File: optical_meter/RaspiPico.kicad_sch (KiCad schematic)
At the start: 7 parts, among them J4 Conn_02x03, U4 Pico

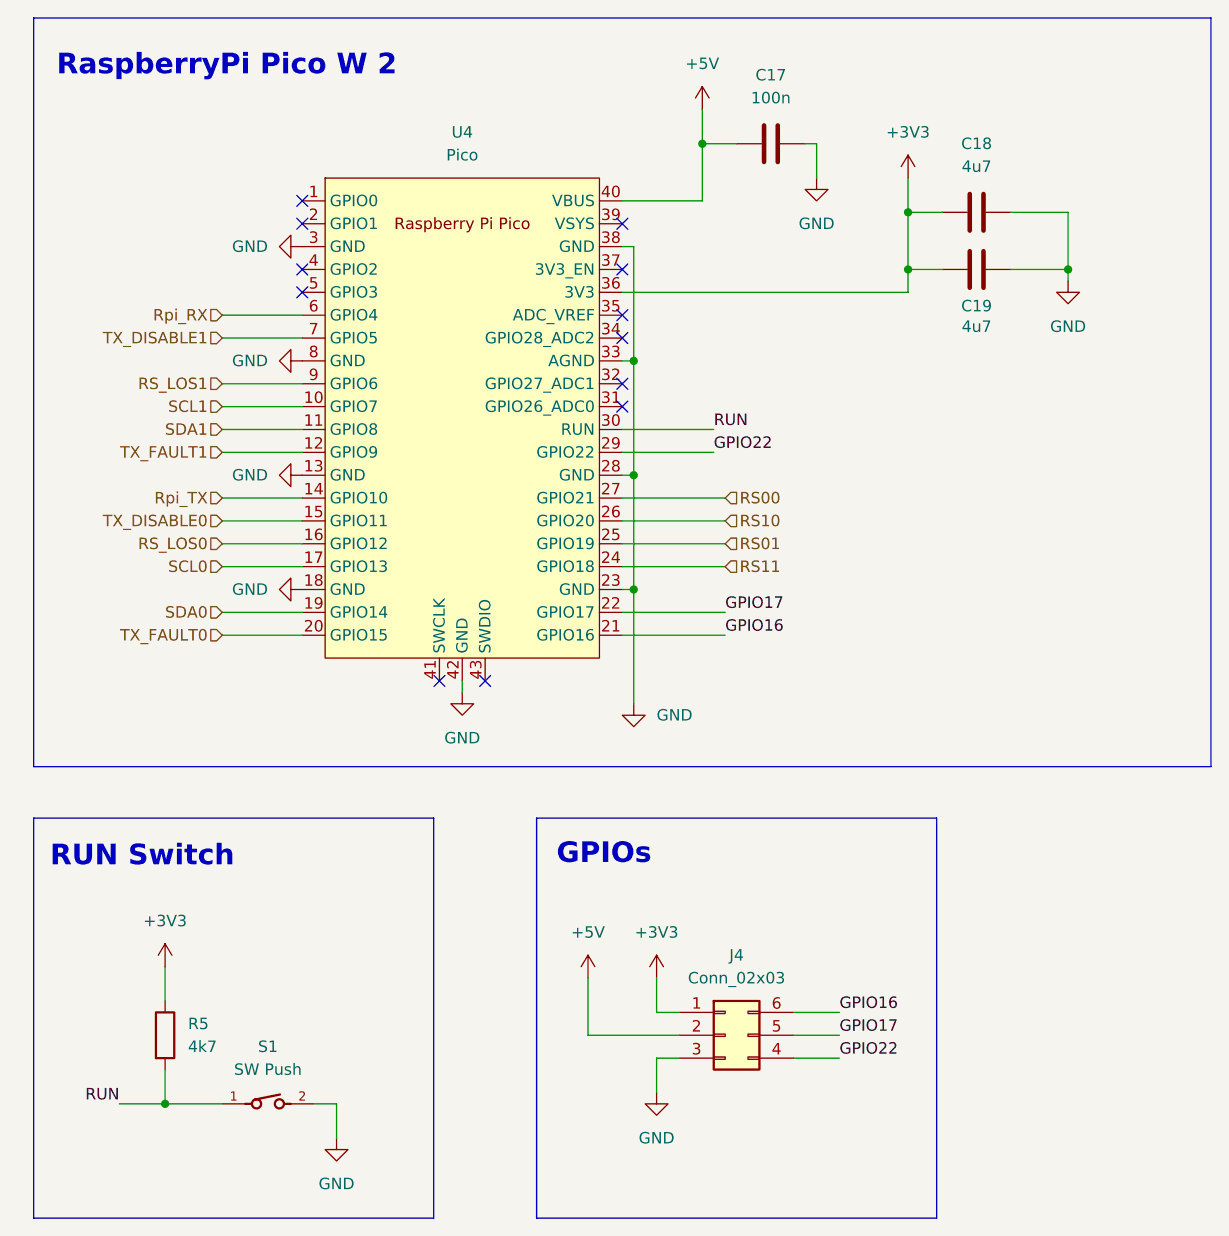
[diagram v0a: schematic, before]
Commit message: Cosmetic changes to schematic sheet
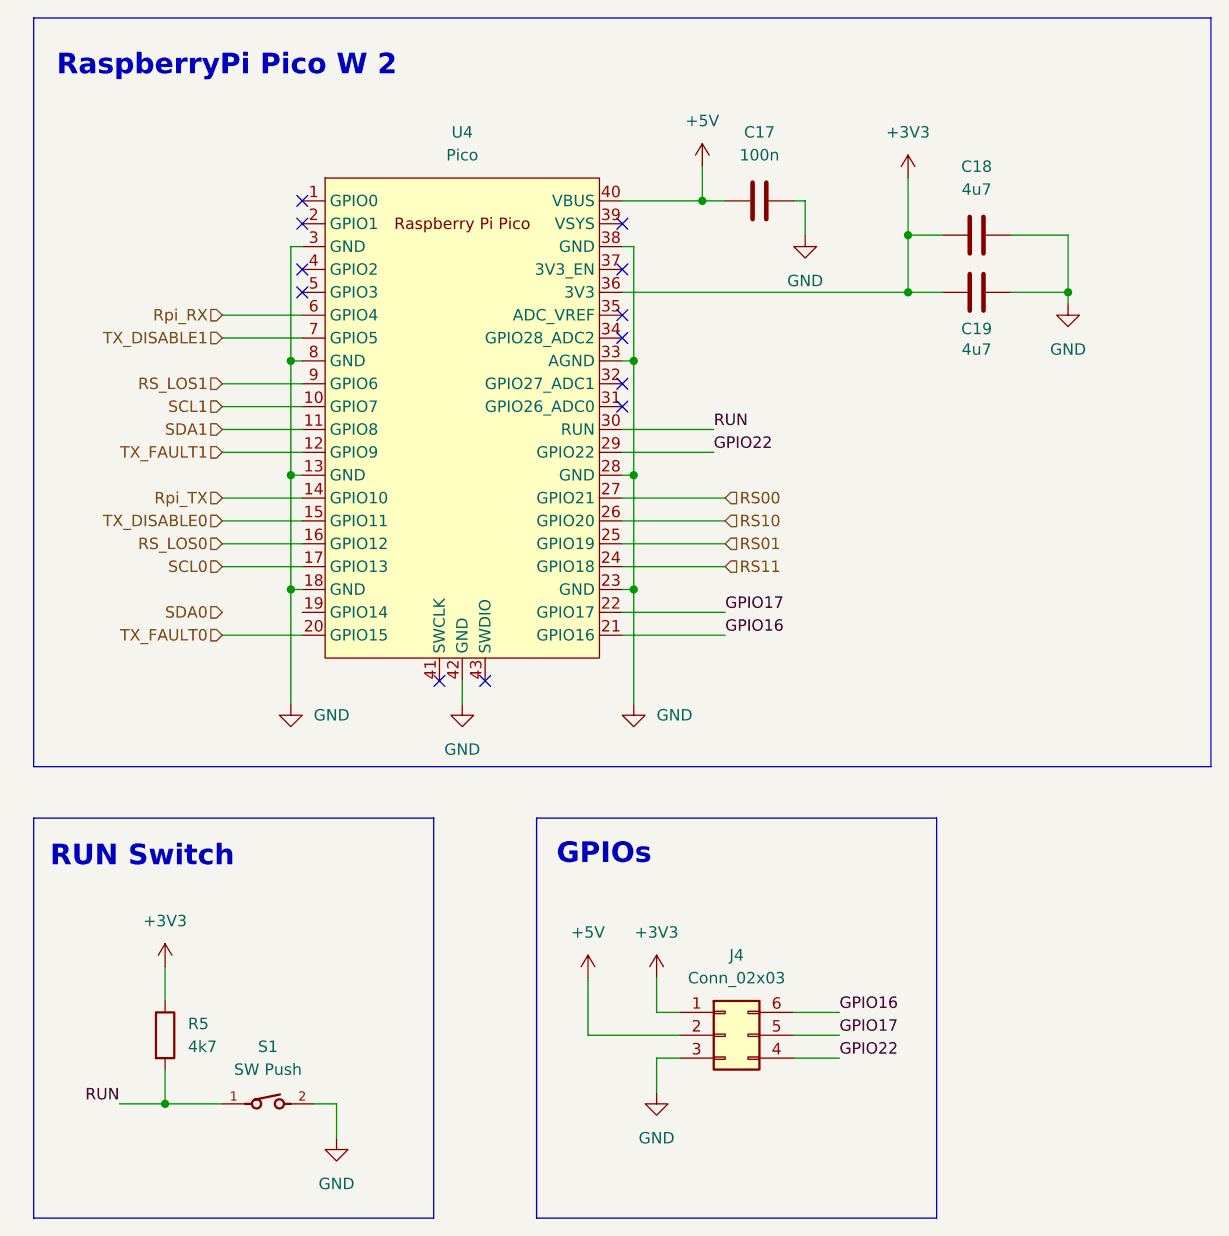
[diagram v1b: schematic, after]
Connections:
- net SDA0: no longer U4.19 (GPIO14)
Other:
- moved on the sheet: C17, C18, C19
